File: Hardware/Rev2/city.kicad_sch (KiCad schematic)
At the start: 294 parts, among them U4 AW20216S, U5 AW20216S, U6 AW20216S

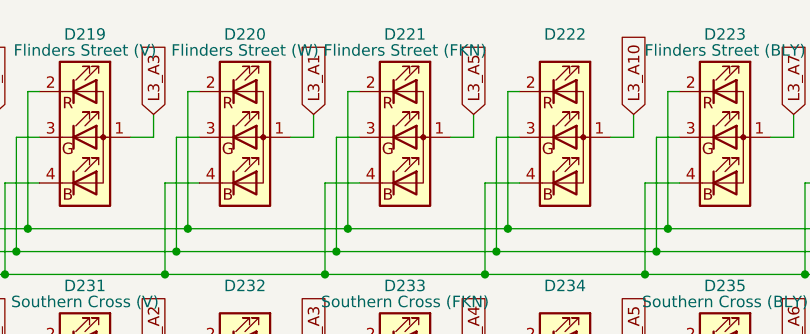
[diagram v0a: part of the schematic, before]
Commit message: fix Armadale, Toorak and Hawksburn (Frankston line) LED wiring, and add Northern group LED offsets
will need to run bodge wires for 1st batch boards
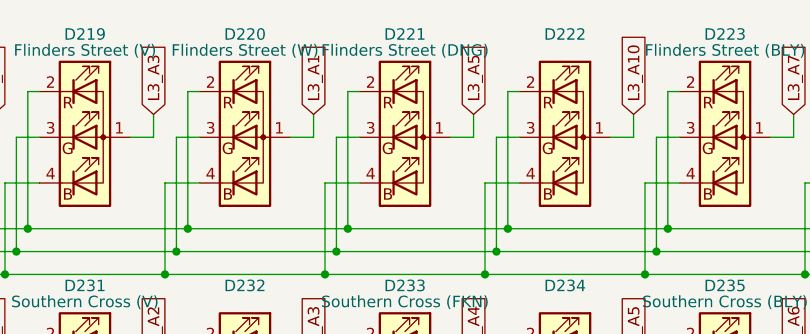
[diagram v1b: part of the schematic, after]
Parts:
- D221: Station Flinders Street (FKN) -> Flinders Street (DNG)
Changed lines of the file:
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@@
 			)
 		)
-		(property "Station" "Flinders Street (FKN)"
+		(property "Station" "Flinders Street (DNG)"
 			(at 199.39 19.558 0)
 			(effects

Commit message: fix Shepparton LED wiring
same stuff as before :(
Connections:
- net L5_A0: no longer D415.1 (A)
- net L5_A1: now also D415.1 (A)
- net L5_A10: no longer D420.1 (A)
- net L5_A11: now also D419.1 (A)
- net L5_A2: no longer D416.1 (A)
- net L5_A3: now also D416.1 (A)
- net L5_A4: no longer D417.1 (A)
- net L5_A5: now also D417.1 (A)
- net L5_A6: no longer D418.1 (A)
- net L5_A7: now also D418.1 (A)
- net L5_A8: no longer D419.1 (A)
- net L5_A9: now also D420.1 (A)
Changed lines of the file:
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@@
 		)
 	)
-	(global_label "L5_A6"
+	(global_label "L5_A7"
 		(shape input)
 		(at 534.67 166.37 90)
@@
 		)
 	)
-	(global_label "L5_A4"
+	(global_label "L5_A5"
 		(shape input)
 		(at 516.89 166.37 90)
@@
 		)
 	)
-	(global_label "L5_A10"
+	(global_label "L5_A9"
 		(shape input)
 		(at 570.23 166.37 90)
@@
 		)
 		(property "Intersheetrefs" "${INTERSHEET_REFS}"
-			(at 570.23 156.672 90)
+			(at 570.23 157.8815 90)
 			(effects
 				(font
@@
 		)
 	)
-	(global_label "L5_A0"
+	(global_label "L5_A1"
 		(shape input)
 		(at 481.33 166.37 90)
@@
 		)
 	)
-	(global_label "L5_A2"
+	(global_label "L5_A3"
 		(shape input)
 		(at 499.11 166.37 90)
@@
 		)
 	)
-	(global_label "L5_A8"
+	(global_label "L5_A11"
 		(shape input)
 		(at 552.45 166.37 90)
@@
 		)
 		(property "Intersheetrefs" "${INTERSHEET_REFS}"
-			(at 552.45 157.8815 90)
+			(at 552.45 156.672 90)
 			(effects
 				(font

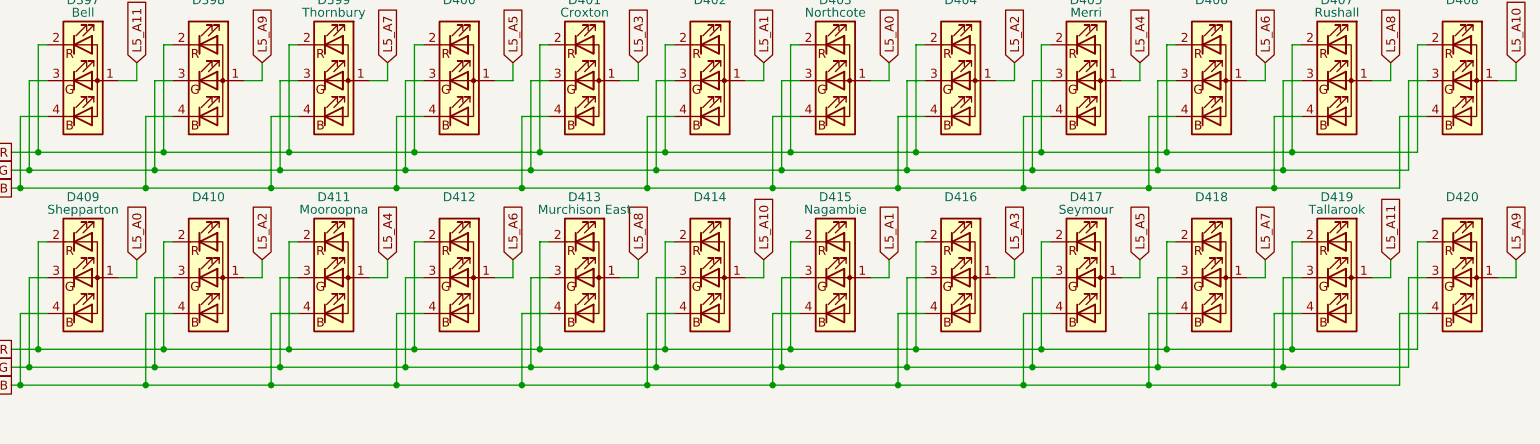
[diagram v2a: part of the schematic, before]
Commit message: revision 2B board: fixed SD card wiring
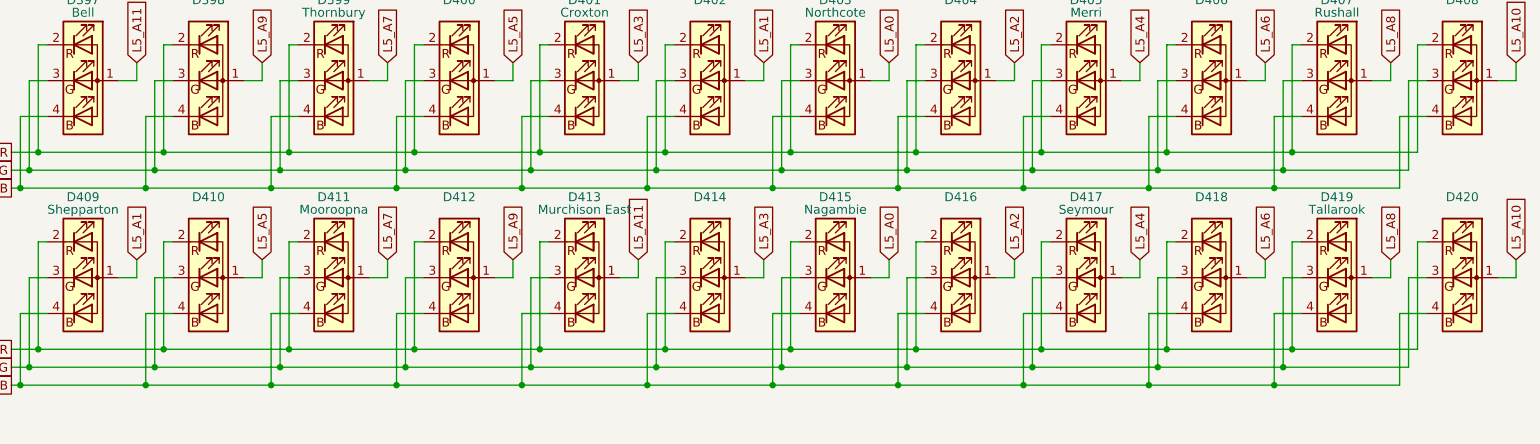
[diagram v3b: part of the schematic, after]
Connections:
- net L5_A0: now also D415.1 (A); no longer D409.1 (A)
- net L5_A1: now also D409.1 (A); no longer D415.1 (A)
- net L5_A10: now also D420.1 (A); no longer D414.1 (A)
- net L5_A11: now also D413.1 (A); no longer D419.1 (A)
- net L5_A2: now also D416.1 (A); no longer D410.1 (A)
- net L5_A3: now also D414.1 (A); no longer D416.1 (A)
- net L5_A4: now also D417.1 (A); no longer D411.1 (A)
- net L5_A5: now also D410.1 (A); no longer D417.1 (A)
- net L5_A6: now also D418.1 (A); no longer D412.1 (A)
- net L5_A7: now also D411.1 (A); no longer D418.1 (A)
- net L5_A8: now also D419.1 (A); no longer D413.1 (A)
- net L5_A9: now also D412.1 (A); no longer D420.1 (A)
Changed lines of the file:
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@@
 		)
 	)
-	(global_label "L5_A2"
+	(global_label "L5_A5"
 		(shape input)
 		(at 392.43 166.37 90)
@@
 		)
 	)
-	(global_label "L5_A7"
+	(global_label "L5_A6"
 		(shape input)
 		(at 534.67 166.37 90)
@@
 		)
 	)
-	(global_label "L5_A5"
+	(global_label "L5_A4"
 		(shape input)
 		(at 516.89 166.37 90)
@@
 		)
 	)
-	(global_label "L5_A9"
+	(global_label "L5_A10"
 		(shape input)
 		(at 570.23 166.37 90)
@@
 		)
 		(property "Intersheetrefs" "${INTERSHEET_REFS}"
-			(at 570.23 157.8815 90)
+			(at 570.23 156.672 90)
 			(effects
 				(font
@@
 		)
 	)
-	(global_label "L5_A0"
+	(global_label "L5_A1"
 		(shape input)
 		(at 374.65 166.37 90)
@@
 		)
 	)
-	(global_label "L5_A6"
+	(global_label "L5_A9"
 		(shape input)
 		(at 427.99 166.37 90)
@@
 		)
 	)
-	(global_label "L5_A1"
+	(global_label "L5_A0"
 		(shape input)
 		(at 481.33 166.37 90)
@@
 		)
 	)
-	(global_label "L5_A3"
+	(global_label "L5_A2"
 		(shape input)
 		(at 499.11 166.37 90)
@@
 		)
 	)
-	(global_label "L5_A4"
+	(global_label "L5_A7"
 		(shape input)
 		(at 410.21 166.37 90)
@@
 		)
 	)
-	(global_label "L5_A10"
+	(global_label "L5_A3"
 		(shape input)
 		(at 463.55 166.37 90)
@@
 		)
 		(property "Intersheetrefs" "${INTERSHEET_REFS}"
-			(at 463.55 156.672 90)
+			(at 463.55 157.8815 90)
 			(effects
 				(font
@@
 		)
 	)
-	(global_label "L5_A8"
+	(global_label "L5_A11"
 		(shape input)
 		(at 445.77 166.37 90)
@@
 		)
 		(property "Intersheetrefs" "${INTERSHEET_REFS}"
-			(at 445.77 157.8815 90)
+			(at 445.77 156.672 90)
 			(effects
 				(font
@@
 		)
 	)
-	(global_label "L5_A11"
+	(global_label "L5_A8"
 		(shape input)
 		(at 552.45 166.37 90)
@@
 		)
 		(property "Intersheetrefs" "${INTERSHEET_REFS}"
-			(at 552.45 156.672 90)
+			(at 552.45 157.8815 90)
 			(effects
 				(font

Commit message: rev.2c revised PCB layout, final
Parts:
- R187, R188, R189: MPN C2930231 -> C15401
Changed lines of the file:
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@@
 			)
 		)
-		(property "MPN" "C2930231"
+		(property "MPN" "C15401"
 			(at 34.29 146.05 90)
 			(effects
@@
 			)
 		)
-		(property "MPN" "C2930231"
+		(property "MPN" "C15401"
 			(at 34.29 236.22 90)
 			(effects
@@
 			)
 		)
-		(property "MPN" "C2930231"
+		(property "MPN" "C15401"
 			(at 34.29 55.88 90)
 			(effects
